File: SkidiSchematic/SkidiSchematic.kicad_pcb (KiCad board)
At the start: 2 copper layers, 44 x 75 mm, 16 parts, among them J1 L-MTR, J2 BUCKET, J3 R-MTR, J4 CLAW, J5 ARM, J6 LIGHTS, J7 TX0, J8 RX0, SW1 SW_SPDT_312, U2 DRV8833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

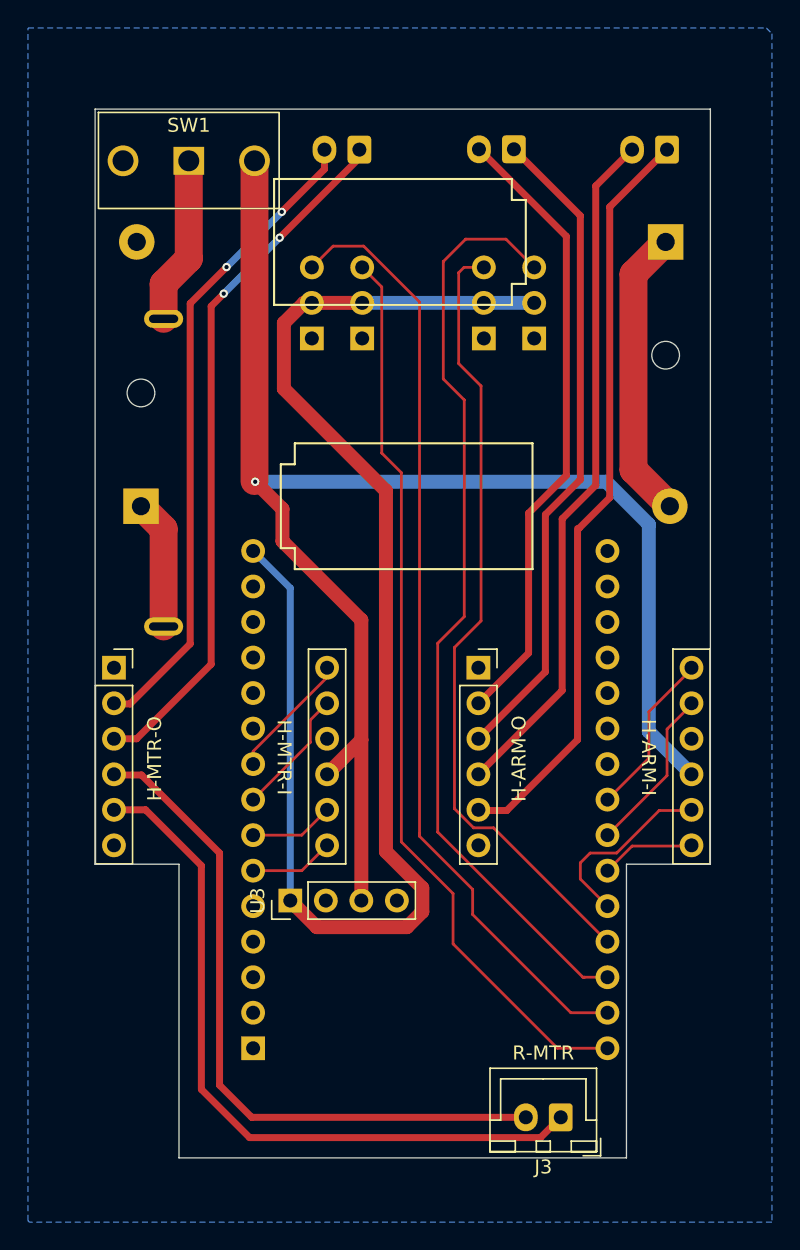
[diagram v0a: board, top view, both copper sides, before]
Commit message: Move switch to the other PCB side
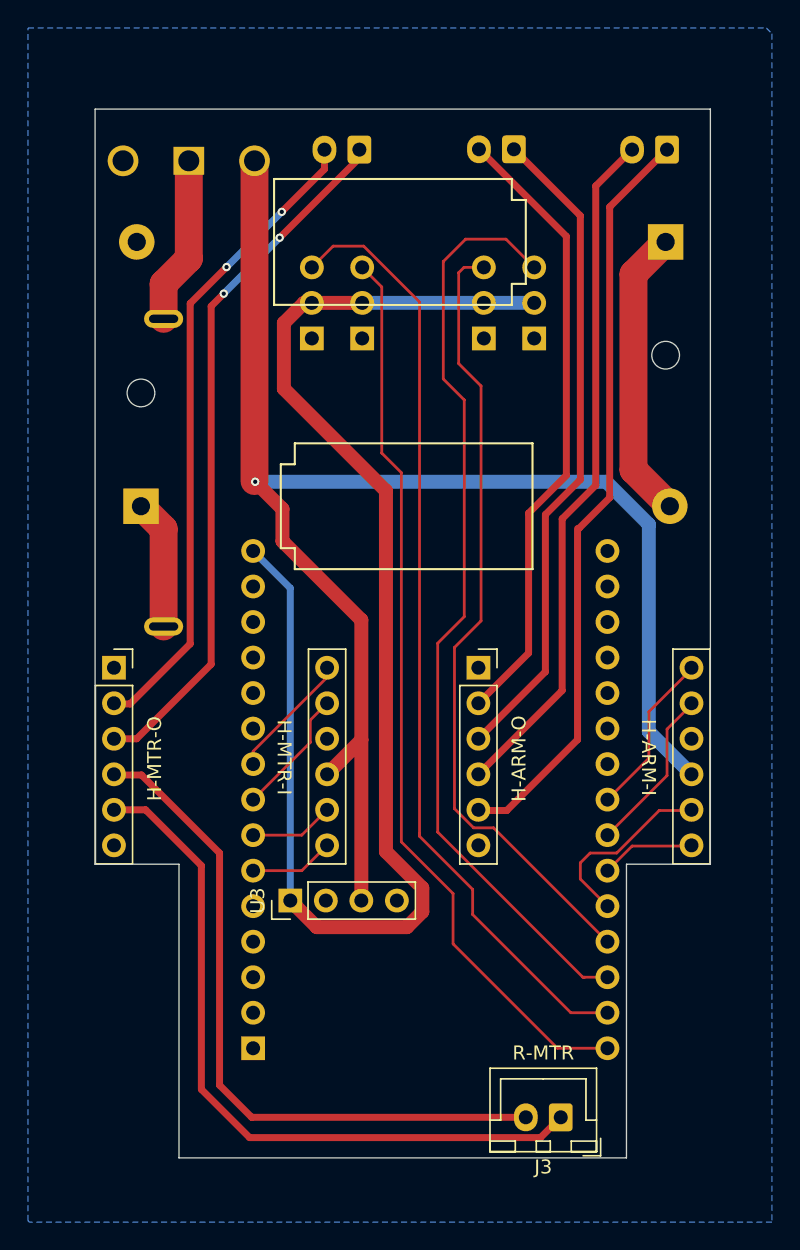
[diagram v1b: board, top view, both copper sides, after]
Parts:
- SW1: moved to B.Cu
